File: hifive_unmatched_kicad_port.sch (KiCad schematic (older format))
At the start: 0 parts

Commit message: Project update
Schematic capture update.
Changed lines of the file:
@@
 S 24200 2850 1750 600
 U 61454C87
-F0 "fu740_dd4" 50
+F0 "fu740_ddr4" 50
 F1 "fu740_ddr4.sch" 50
 $EndSheet

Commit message: Project update
Schematic capture update.
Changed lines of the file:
@@
 $Descr A2 23386 16535
 encoding utf-8
-Sheet 1 6
+Sheet 1 7
 Title ""
 Date ""
@@
 F1 "fu740_power.sch" 50
 $EndSheet
+$Sheet
+S 24200 6300 1750 650
+U 6145B860
+F0 "ddr4x8_32bit" 50
+F1 "ddr4x8_32bit_.sch" 50
+$EndSheet
 $EndSCHEMATC

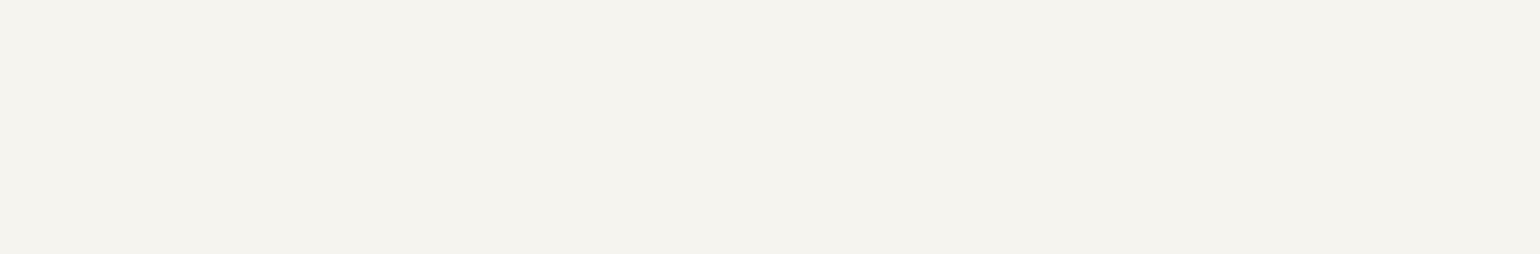
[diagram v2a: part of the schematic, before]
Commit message: Schematic capture update.
Schematic capture update.  DDR4 section updated.
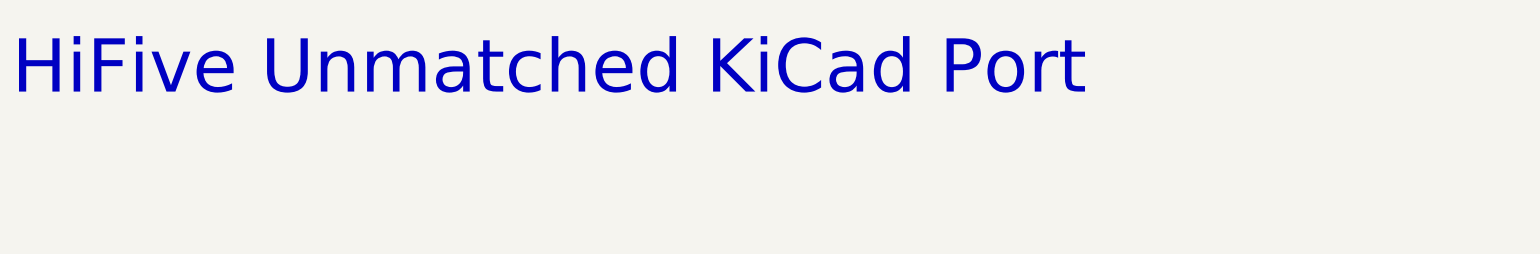
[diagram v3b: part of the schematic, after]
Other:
- note added: "HiFive Unmatched KiCad Port"
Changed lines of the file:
@@
 F1 "ddr4x8_32bit_.sch" 50
 $EndSheet
+Text Notes 7850 1200 0    354  ~ 0
+HiFive Unmatched KiCad Port
 $EndSCHEMATC
